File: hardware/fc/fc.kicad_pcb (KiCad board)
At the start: 6 copper layers, 35 x 35 mm, 94 parts, among them J1 USB4110-GF-A, J2 Micro_SD_Card_Det1, J3 FROM_ESC, J4 CAM, J5 CAM_CC, J6 ELRS, J7 VTX, SW1 Push, U1 TPS7A8101DRBR, U10 TPS2116DRL, U11 OPA354AIDBVR, U12 RP2354A, U2 TPS7A8101DRBR, U3 LMR51420YFDDCR, U4 USBLC6-2SC6, U5 EMIF06-MSD02N16, U6 LSM6DSK320X, U8 TS5A3159ADCK, U9 TLV7031DCKR, X1 ABM8-272-T3

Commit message: fc: prelim OSD layout
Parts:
- C34, R19, R20: moved to B.Cu
- moved U12 66.1 mm to (163.0, 110.6)
- moved C34 51.7 mm to (162.9, 100.8), turned to -90 degrees
- moved R19 48.4 mm to (164.4, 100.3), turned to 180 degrees
- moved R20 47.7 mm to (164.4, 101.4)
- moved U9 41.5 mm to (164.4, 119.5), turned to 0 degrees
- moved U8 36.7 mm to (159.5, 118.2)
- moved R16 35.0 mm to (161.3, 120.4), turned to -90 degrees
- moved C28 33.6 mm to (165.8, 121.3), turned to 0 degrees
- moved U11 32.6 mm to (154.8, 118.6)
- moved R9 31.2 mm to (159.8, 119.9)
- moved R11 31.0 mm to (160.3, 116.1), turned to -90 degrees
- moved C26 30.3 mm to (162.3, 120.4), turned to -90 degrees
- moved R12 30.2 mm to (159.3, 116.1), turned to 90 degrees
- moved D1 30.1 mm to (161.8, 117.7)
- moved C27 29.8 mm to (162.0, 118.9)
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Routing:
- net Net-(U11-OUT): track 0.00 -> 5.87 mm
- net Net-(C26-Pad1): track 0.00 -> 2.84 mm
- net Net-(D1-K): track 0.00 -> 2.42 mm
- net Net-(U11-IN-): track 0.00 -> 2.26 mm
- net /OSD/VIDEO_IN: track 0.00 -> 2.07 mm

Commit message: fc: schematic footprint changes
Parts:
- H1, H2, H3, H4: footprint Stratus:Mount_M3_K0.5 -> MountingHole:MountingHole_3.2mm_M3
- U9: footprint Package_TO_SOT_SMD:SOT-353_SC-70-5 -> Package_TO_SOT_SMD:SOT-363_SC-70-6
- moved U6 54.0 mm to (178.9, 79.8), turned to 180 degrees
- moved C20 51.3 mm to (179.9, 77.8)
- moved C19 48.0 mm to (176.6, 79.6), turned to -90 degrees
- moved C9 16.1 mm to (161.5, 76.9)
- moved C10 15.9 mm to (161.5, 78.0)
- moved C8 15.9 mm to (161.0, 75.4), turned to -90 degrees
- moved C7 12.3 mm to (155.2, 76.4), turned to 180 degrees
- moved C6 12.0 mm to (155.2, 77.5), turned to 180 degrees
- moved R4 11.7 mm to (163.1, 75.4), turned to 90 degrees
- moved R3 11.5 mm to (162.1, 75.4), turned to -90 degrees
- moved U2 3.52 mm to (158.3, 76.8), turned to 180 degrees
- turned U12 to 90 degrees
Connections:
- J2 pad 1: unconnected-(J2-DAT2-Pad1) -> Net-(J2-DAT2)
- J2 pad 8: unconnected-(J2-DAT1-Pad8) -> Net-(J2-DAT1)
- U10 pad 4: GND -> V_BUS
- U10 pad 5: GND -> V_BUS
- U12 pad 12: unconnected-(U12-GPIO8-Pad12) -> /Sensors/IMU.INT
- U12 pad 13: /Sensors/IMU.INT -> /Sensors/IMU.nCS
- U12 pad 17: /Sensors/IMU.nCS -> unconnected-(U12-GPIO13-Pad17)
- U5 pad 3: unconnected-(U5-DAT2_IN-Pad3) -> Net-(J2-DAT2)
- U5 pad 8: unconnected-(U5-DAT1_IN-Pad8) -> Net-(J2-DAT1)
- U6 pad 1: /Sensors/IMU_MISO -> /Sensors/IMU.MISO
- U6 pad 12: /Sensors/IMU_nCS -> /Sensors/IMU.nCS
- U6 pad 13: /Sensors/IMU_SCLK -> /Sensors/IMU.SCLK
- U6 pad 14: /Sensors/IMU_MOSI -> /Sensors/IMU.MOSI
- U6 pad 2: GND -> unconnected-(U6-SDX-Pad2)
- U6 pad 3: GND -> unconnected-(U6-SCX-Pad3)
- U6 pad 4: /Sensors/IMU_INT -> /Sensors/IMU.INT

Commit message: fc: prelim MCU and IMU layout
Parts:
- moved SW1 68.4 mm to (173.0, 111.0), turned to -90 degrees
- moved C20 43.2 mm to (160.1, 116.2), turned to -90 degrees
- moved U6 41.0 mm to (158.0, 115.1), turned to 90 degrees
- moved C19 37.9 mm to (158.2, 112.8), turned to 180 degrees
- moved R4 37.5 mm to (160.2, 112.8), turned to 0 degrees
- moved R3 36.4 mm to (160.2, 111.8), turned to 180 degrees
- moved C8 35.3 mm to (160.2, 110.7), turned to 180 degrees
- moved C9 35.0 mm to (158.2, 111.8), turned to 180 degrees
- moved C10 32.9 mm to (158.2, 110.7), turned to 180 degrees
- moved U2 31.2 mm to (158.8, 108.0), turned to 90 degrees
- moved C7 28.8 mm to (159.2, 104.9), turned to 90 degrees
- moved C6 27.6 mm to (158.2, 104.9), turned to 90 degrees
- moved U12 2.43 mm to (165.4, 110.7), turned to 0 degrees
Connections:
- U12 pad 12: /Sensors/IMU.INT -> unconnected-(U12-GPIO8-Pad12)
- U12 pad 17: unconnected-(U12-GPIO13-Pad17) -> /Sensors/IMU.INT
- U12 pad 18: /OSD_EN -> /OSD_W
- U12 pad 27: /OSD_W -> /OSD_EN

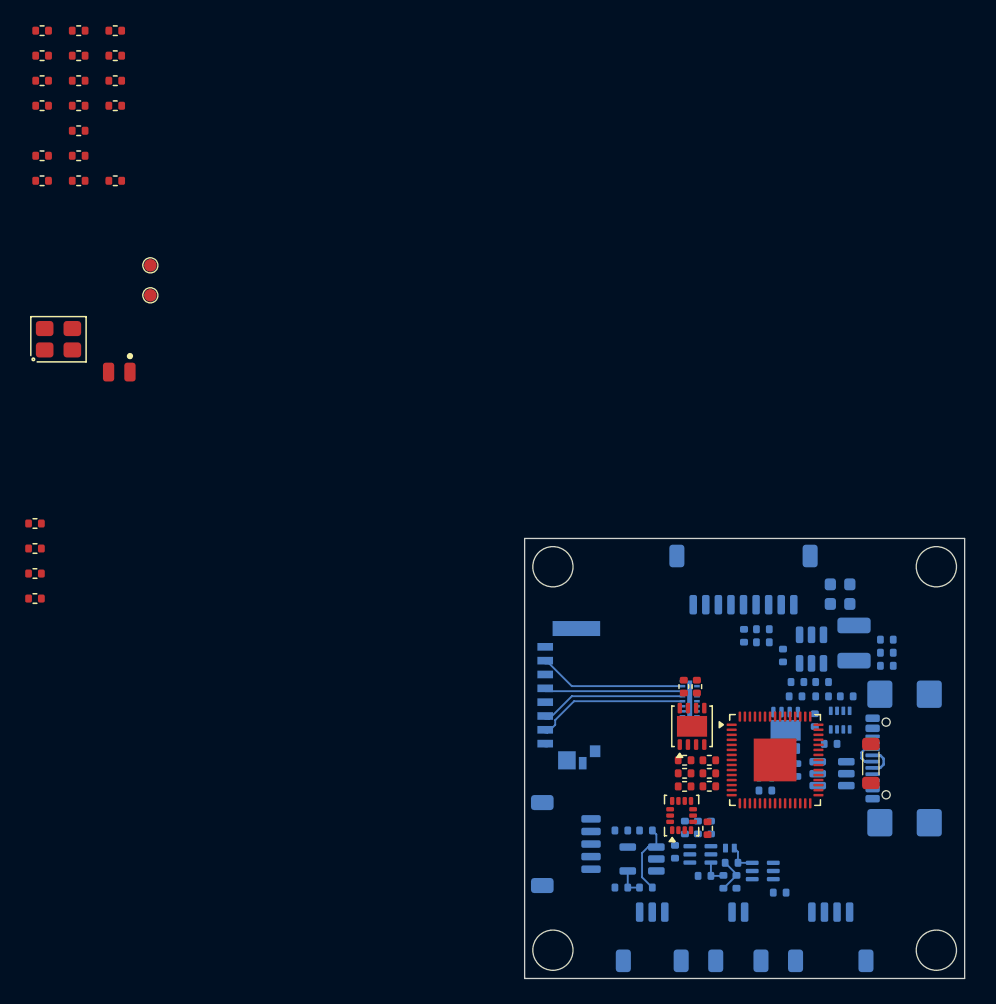
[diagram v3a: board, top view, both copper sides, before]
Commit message: fc: prelim MCU + IMU
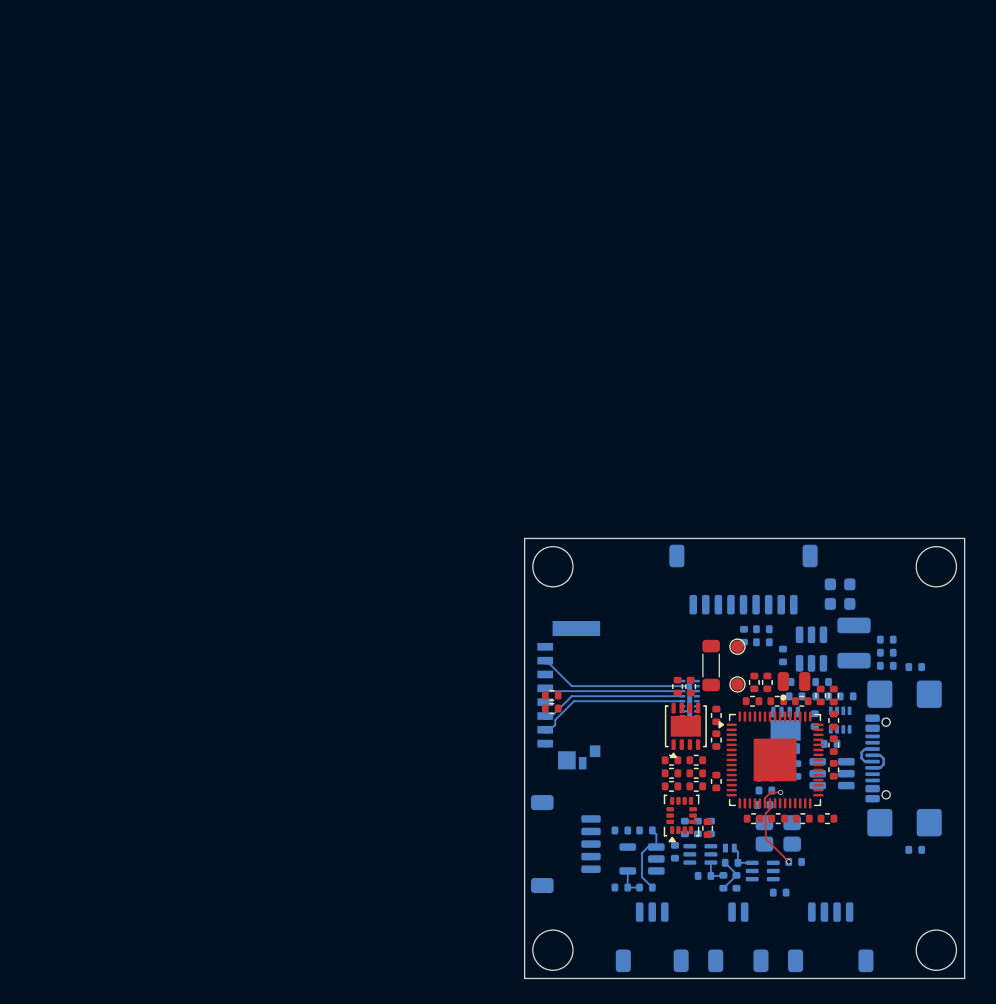
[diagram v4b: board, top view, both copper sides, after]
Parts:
- added C46: 0.1uF, Stratus:C_0402, F.Cu at (163.6, 106.0)
- C32, C33, R7, R8, X1: moved to B.Cu
- moved C33 84.9 mm to (167.0, 118.8)
- moved C37 83.8 mm to (165.7, 115.4)
- moved C22 82.2 mm to (170.1, 105.6), turned to 90 degrees
- moved C44 82.0 mm to (170.1, 111.5), turned to -90 degrees
- moved C38 81.3 mm to (170.1, 109.5), turned to 90 degrees
- moved C32 81.3 mm to (164.5, 114.3), turned to 180 degrees
- moved C43 78.2 mm to (169.6, 115.4)
- moved C42 78.1 mm to (167.6, 115.4)
- moved C45 77.9 mm to (170.1, 107.6), turned to 90 degrees
- moved C23 77.8 mm to (165.6, 106.0), turned to 180 degrees
- moved C41 76.7 mm to (163.7, 115.4), turned to 180 degrees
- moved C35 74.4 mm to (167.6, 106.0)
- moved C40 73.9 mm to (160.8, 112.4), turned to -90 degrees
- moved R8 72.8 mm to (176.6, 117.9), turned to 180 degrees
- moved C39 71.6 mm to (160.8, 107.2), turned to 90 degrees
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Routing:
- net Net-(U12-XOUT): track 0.00 -> 5.55 mm, vias 0 -> 1
- net Net-(U12-XIN): track 0.00 -> 1.84 mm, vias 0 -> 1

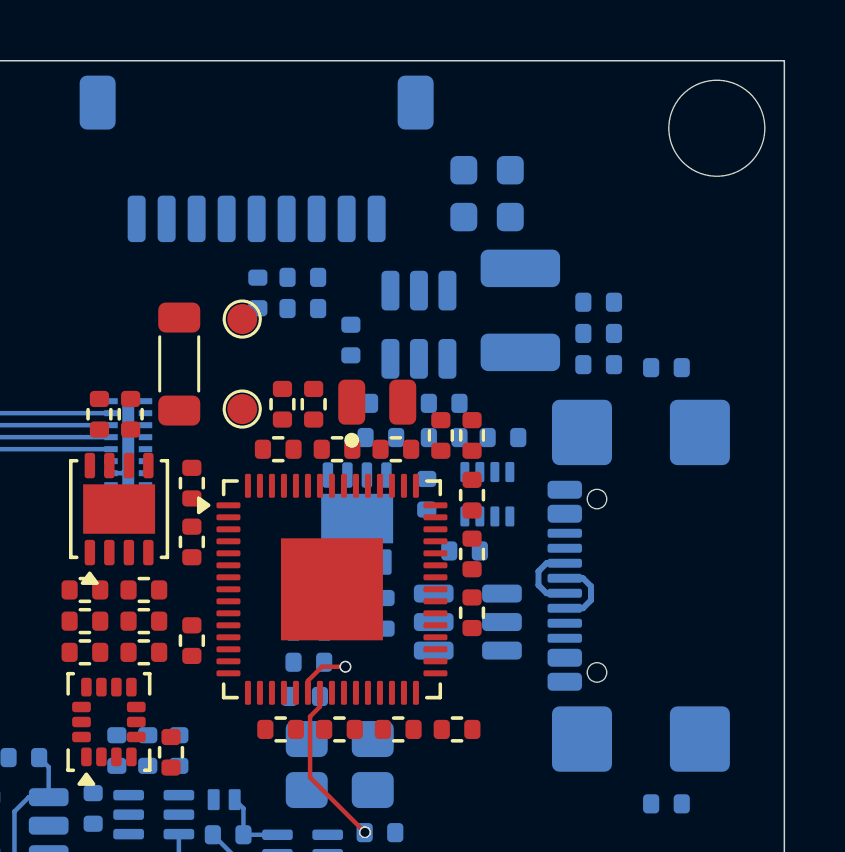
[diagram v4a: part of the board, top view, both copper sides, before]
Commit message: fc: add power pours
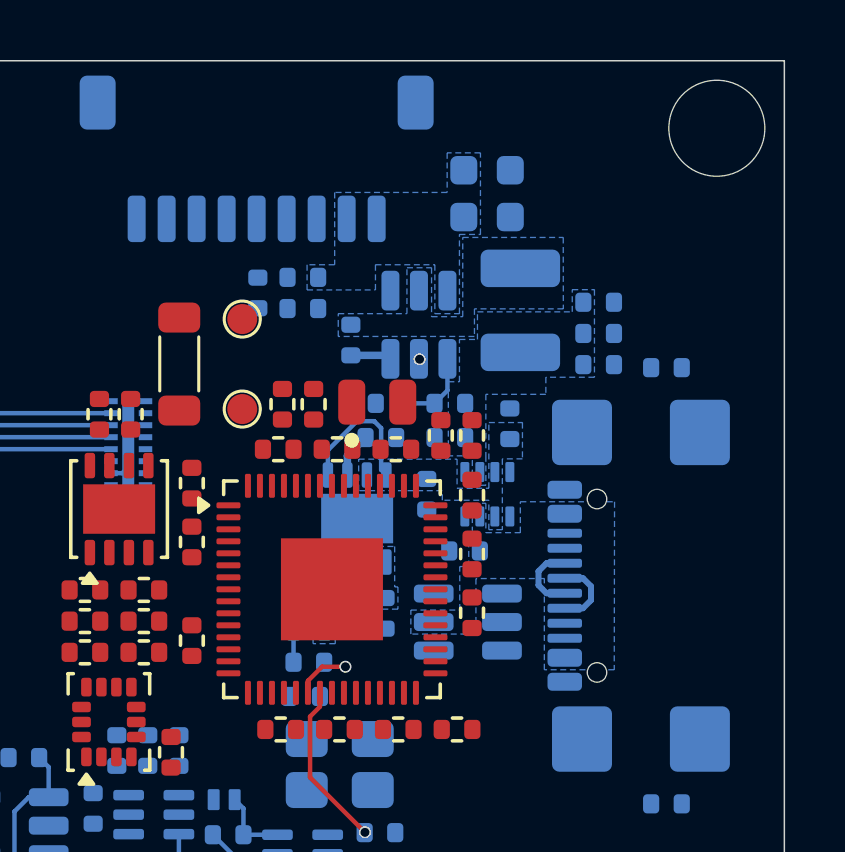
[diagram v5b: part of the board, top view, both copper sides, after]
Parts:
- moved C3 1.04 mm to (164.7, 112.1), turned to 180 degrees
- moved R1 1.04 mm to (164.7, 111.1), turned to 180 degrees
- moved C31 0.51 mm to (171.3, 105.2), turned to 90 degrees
- moved C30 0.19 mm to (169.3, 105.7)
- moved R5 0.19 mm to (169.3, 104.5)
- moved R6 0.19 mm to (167.4, 104.5)
- turned R2 to 0 degrees
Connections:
- U10 pad 4: V_BUS -> GND
- U10 pad 5: V_BUS -> GND
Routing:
- net V_5V: track 0.00 -> 4.73 mm
- net Net-(U1-FB/SNS): track 0.00 -> 4.55 mm
- net Net-(U3-FB): track 0.00 -> 2.60 mm
- net Net-(U1-NR): track 0.00 -> 1.50 mm
- net Net-(U3-BOOT): track 0.00 -> 1.37 mm
- net V_BAT: track 0.00 -> 0.03 mm, vias 0 -> 1
- added copper zone on B.Cu, net /Power/V_5V_BUCK
- added copper zone on B.Cu, net Net-(U3-SW)
- added copper zone on B.Cu, net V_3V3
- added copper zone on B.Cu, net V_5V
- added copper zone on B.Cu, net V_BAT
- added copper zone on B.Cu, net V_BUS

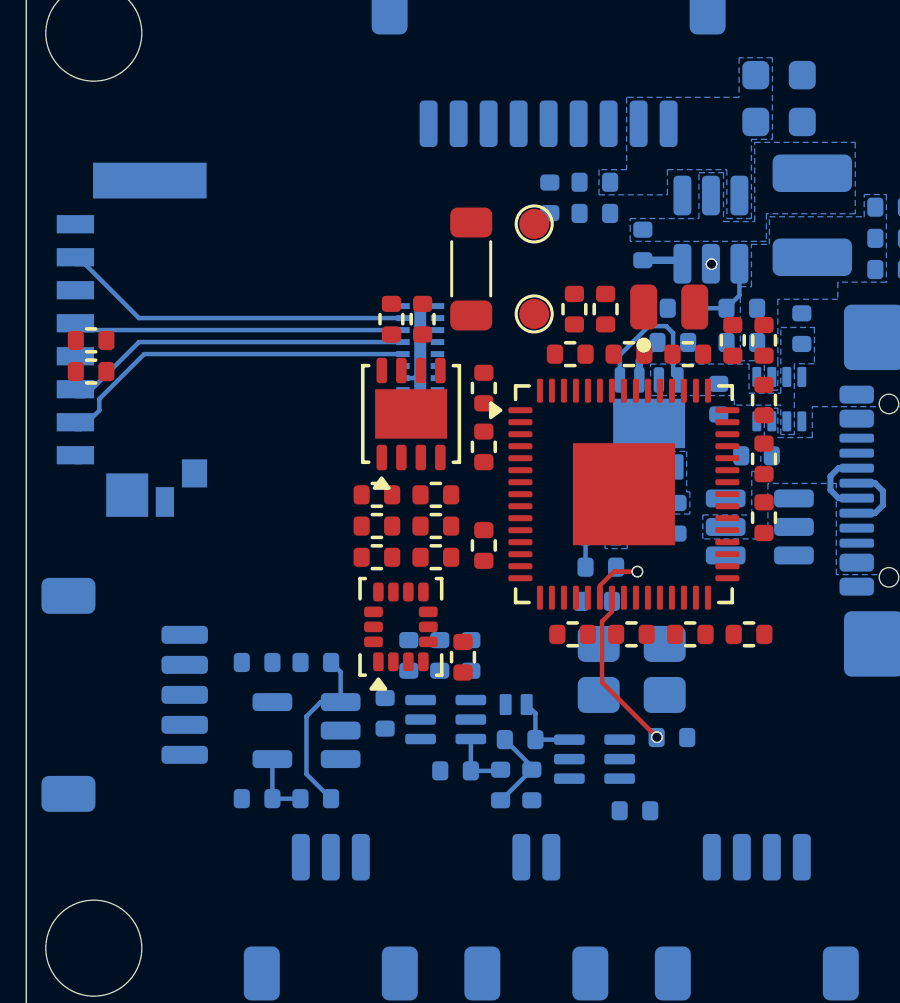
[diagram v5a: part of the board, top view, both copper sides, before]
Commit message: fc: OSD
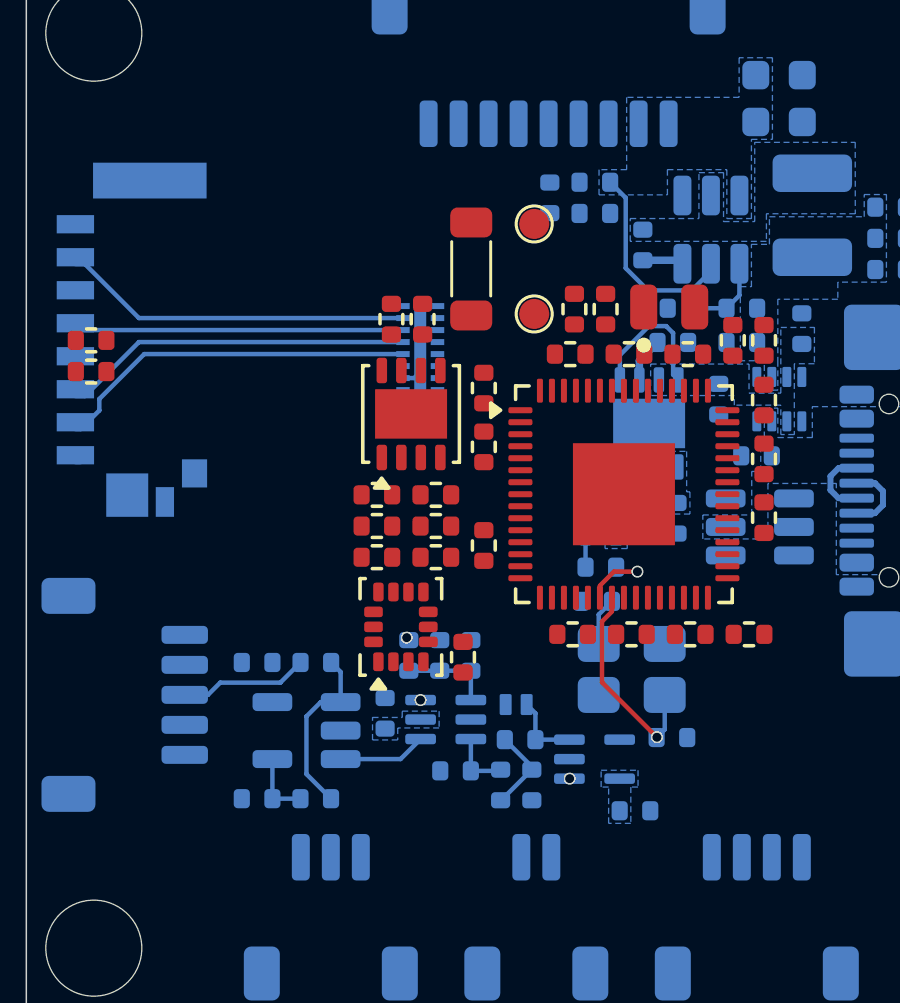
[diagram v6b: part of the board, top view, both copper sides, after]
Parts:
- U9: footprint Package_TO_SOT_SMD:SOT-363_SC-70-6 -> Package_TO_SOT_SMD:SOT-353_SC-70-5
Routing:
- net V_BAT: track 0.03 -> 6.76 mm, vias 1 -> 0
- net /OSD/VIDEO_OUT: track 0.00 -> 4.31 mm
- net Net-(R10-Pad1): track 0.00 -> 3.05 mm
- net Net-(U11-IN+): track 0.00 -> 2.94 mm
- net Net-(U12-XIN): track 1.84 -> 3.45 mm
- net Net-(U12-XOUT): track 5.55 -> 7.08 mm
- net /OSD_W: track 0.00 -> 0.11 mm, vias 0 -> 1
- net /OSD_SYNC: track 0.00 -> 0.01 mm, vias 0 -> 1
- net /OSD_EN: vias 0 -> 1

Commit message: fc: layout work
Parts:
- R17, R18: moved to B.Cu
- R7, R8: moved to F.Cu
- moved R7 7.57 mm to (173.7, 110.3)
- moved R8 7.11 mm to (173.7, 111.4)
- moved R17 4.47 mm to (163.4, 109.0), turned to 180 degrees
- moved R18 3.70 mm to (163.4, 108.0), turned to 180 degrees
- moved C2 1.62 mm to (165.4, 105.7), turned to 180 degrees
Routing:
- net V_1V1: track 0.00 -> 27.1 mm, vias 0 -> 5
- net V_3V3: track 0.00 -> 11.0 mm, vias 0 -> 12
- net Net-(U2-FB/SNS): track 0.00 -> 3.86 mm
- net Net-(U12-~{QSPI_SS}): track 0.00 -> 3.46 mm
- net V_5V: track 4.73 -> 7.85 mm
- net Net-(U12-VREG_LX): track 0.00 -> 2.94 mm
- net Net-(U12-VREG_AVDD): track 0.00 -> 2.55 mm
- net Net-(U2-NR): track 0.00 -> 1.22 mm
- net Net-(J1-CC1): track 0.00 -> 0.98 mm, vias 0 -> 1
- net Net-(J1-CC2): track 0.00 -> 0.98 mm, vias 0 -> 1
- net Net-(U12-XIN): track 3.45 -> 4.27 mm
- net Net-(U12-USB_DP): track 0.00 -> 0.33 mm, vias 0 -> 1
- net Net-(U12-USB_DM): track 0.00 -> 0.28 mm, vias 0 -> 1
- net /D+: vias 0 -> 1
- net /D-: vias 0 -> 1
- added copper zone on F.Cu, net V_1V1
- added copper zone on F.Cu, net V_3V3
- added copper zone on F.Cu, net V_5V
- added copper zone on F.Cu, net V_IMU

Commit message: fc: PDN; further layout work
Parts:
- moved R18 1.04 mm to (163.4, 109.0), turned to 0 degrees
- moved R17 1.04 mm to (163.4, 108.0), turned to 0 degrees
- moved SW1 0.15 mm to (160.5, 103.2)
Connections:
- net /Peripherals/ESC_TEL renamed /Peripherals/ESC.TEL
- J3 pad 1: /Peripherals/ESC_M4 -> /Peripherals/ESC.M4
- J3 pad 2: /Peripherals/ESC_M3 -> /Peripherals/ESC.M3
- J3 pad 3: /Peripherals/ESC_M2 -> /Peripherals/ESC.M2
- J3 pad 4: /Peripherals/ESC_M1 -> /Peripherals/ESC.M1
- U5 pad 10: /Peripherals/SD_DAT0 -> /Peripherals/SD.DAT0
- U5 pad 11: /Peripherals/SD_CLK -> /Peripherals/SD.CLK
- U5 pad 12: /Peripherals/SD_CMD -> /Peripherals/SD.CMD
- U5 pad 13: /Peripherals/SD_DAT3 -> /Peripherals/SD.DAT3
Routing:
- net /Peripherals/SD.DAT0: track 0.00 -> 15.8 mm, vias 0 -> 2
- net /Peripherals/SD.CMD: track 0.00 -> 14.3 mm, vias 0 -> 2
- net /Peripherals/SD.DAT3: track 0.00 -> 14.1 mm, vias 0 -> 2
- net /Peripherals/SD.CLK: track 0.00 -> 13.4 mm, vias 0 -> 2
- net /D+: track 0.00 -> 8.17 mm, vias 1 -> 2
- net /Sensors/IMU.MISO: track 0.00 -> 6.53 mm, vias 0 -> 2
- net /Sensors/IMU.MOSI: track 0.00 -> 6.38 mm, vias 0 -> 2
- net /D-: track 0.00 -> 6.33 mm, vias 1 -> 2
- net /Sensors/IMU.nCS: track 0.00 -> 6.30 mm, vias 0 -> 2
- net /Sensors/IMU.INT: track 0.00 -> 6.25 mm, vias 0 -> 2
- net /Sensors/IMU.SCLK: track 0.00 -> 5.74 mm, vias 0 -> 2
- net Net-(U12-USB_DM): track 0.28 -> 5.00 mm
- net Net-(U12-USB_DP): track 0.33 -> 4.25 mm
- net Net-(J1-D+-PadA6): track 2.44 -> 5.41 mm
- net Net-(J1-D--PadA7): track 2.44 -> 4.57 mm
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- added copper zone on In3.Cu, net V_3V3
- added copper zone on In3.Cu, net V_5V
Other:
- board text added: "BOOT"
- board text added: "CLK"
- board text added: "IO"
